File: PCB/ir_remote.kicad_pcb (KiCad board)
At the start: 2 copper layers, 26.2 x 50.5 mm, 22 parts, among them J1 105017-0001, SW1 95C06B3GWRT, U1 ESP32-DOIT-EVALKIT, U2 MCP73832T2DFI/OT, U3 TSOP38238

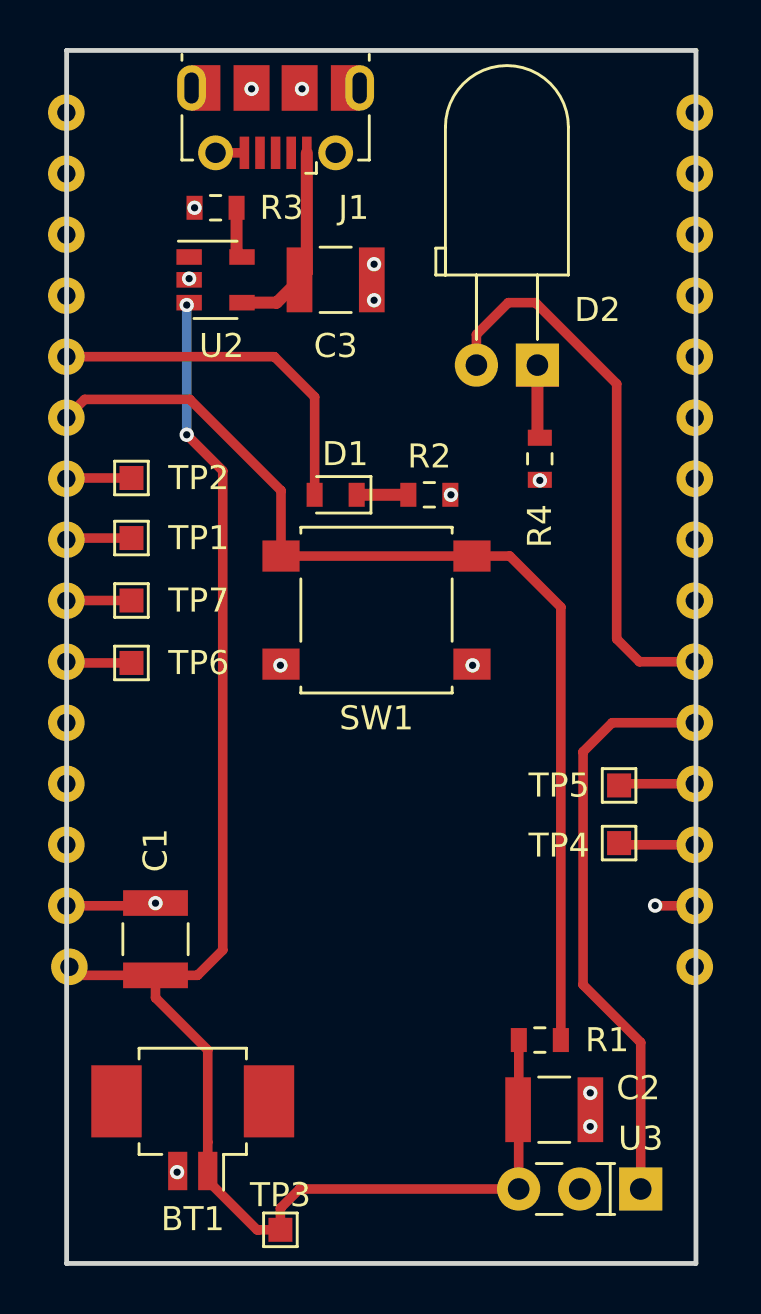
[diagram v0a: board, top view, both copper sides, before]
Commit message: fixed several 3D components and layout gnd via
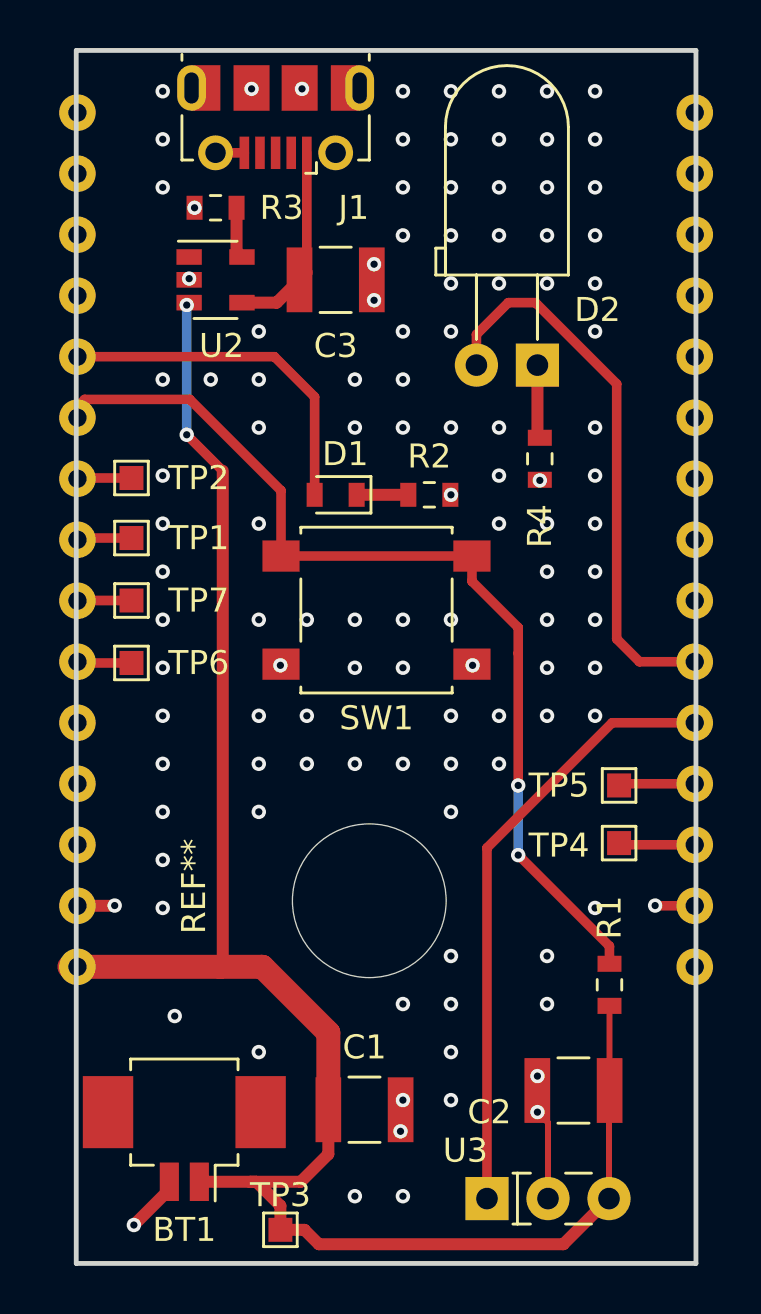
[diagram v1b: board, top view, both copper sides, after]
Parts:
- added REF**: MountingHole_6.4mm_M6, MountingHole:MountingHole_6.4mm_M6, F.Cu at (156.1, 86.4)
- moved C1 11.2 mm to (155.9, 95.1), turned to 0 degrees
- moved U3 6.41 mm to (161.0, 98.8), turned to 0 degrees
- moved R1 3.70 mm to (166.1, 89.9), turned to 270 degrees
- moved C2 1.13 mm to (164.6, 94.3), turned to 180 degrees
- moved BT1 0.57 mm to (148.4, 95.7)
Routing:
- net 4V2: track 65.1 -> 77.0 mm
- net GND: track 6.61 -> 11.1 mm, vias 15 -> 114
- net Net-(R1-Pad1): track 44.1 -> 40.9 mm, vias 0 -> 2
- net Net-(U1-Pad5): track 24.3 -> 25.4 mm
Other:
- board size 26.2 x 50.5 mm -> 25.8 x 50.5 mm

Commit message: minor
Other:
- board text added: "Infrared Remote V0.8"
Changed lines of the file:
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@@
   (general
     (thickness 1.6)
-    (drawings 4)
+    (drawings 5)
     (tracks 198)
     (zones 0)
@@
   (module ir_remote:ESP32-DOIT-EVALKIT (layer B.Cu)
     (at 156.95 63.75)
+    (attr virtual)
     (fp_text reference U1 (at 9.95 -10.15) (layer B.SilkS)
       (effects (font (size 1 1) (thickness 0.15)) (justify mirror))
@@
     (tags "mounting hole 6.4mm no annular m6")
     (attr virtual)
-    (fp_text reference REF** (at -7.3 -0.6 90) (layer F.SilkS)
+    (fp_text reference REF** (at -7.3 -0.6 90) (layer F.SilkS) hide
       (effects (font (size 1 1) (thickness 0.15)))
     )
@@
     (pad 1 np_thru_hole circle (at 0 0) (size 6.4 6.4) (drill 6.4) (layers *.Cu *.Mask))
   )
+  (gr_text "Infrared Remote\nV0.8" (at 150 92.2 90) (layer F.SilkS)
+    (effects (font (size 1.1 1.1) (thickness 0.2)) (justify left))
+  )
   (gr_line (start 143.9 101.5) (end 143.9 51) (layer Edge.Cuts) (width 0.2))
